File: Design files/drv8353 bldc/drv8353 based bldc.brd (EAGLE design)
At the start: 127 x 127 mm, 117 parts, among them IC1 DRV8353RSRGZT, J3 2X6 FEMALE, J4 B06B-HCMKK

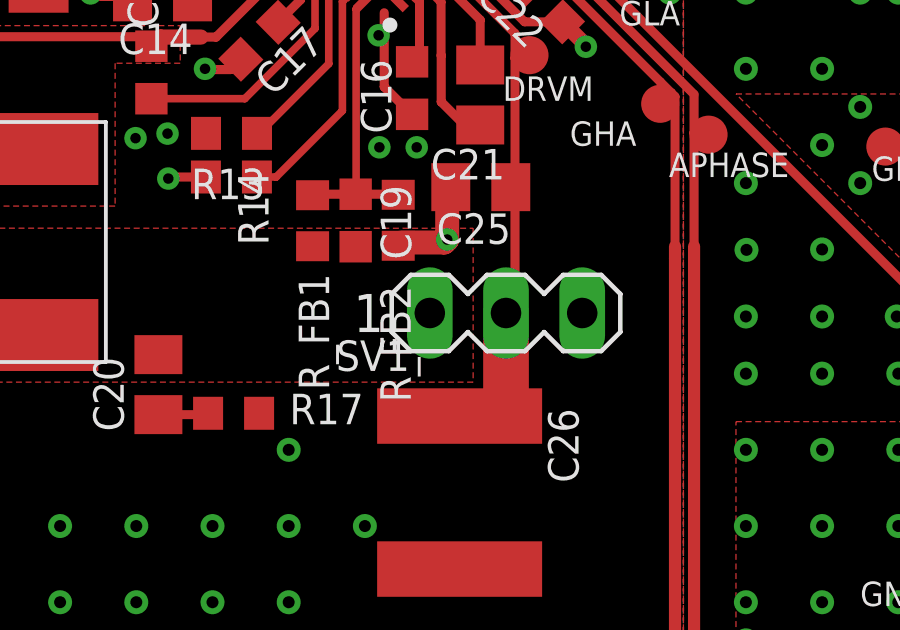
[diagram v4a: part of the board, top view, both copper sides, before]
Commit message: adds 3d  packages for some parts
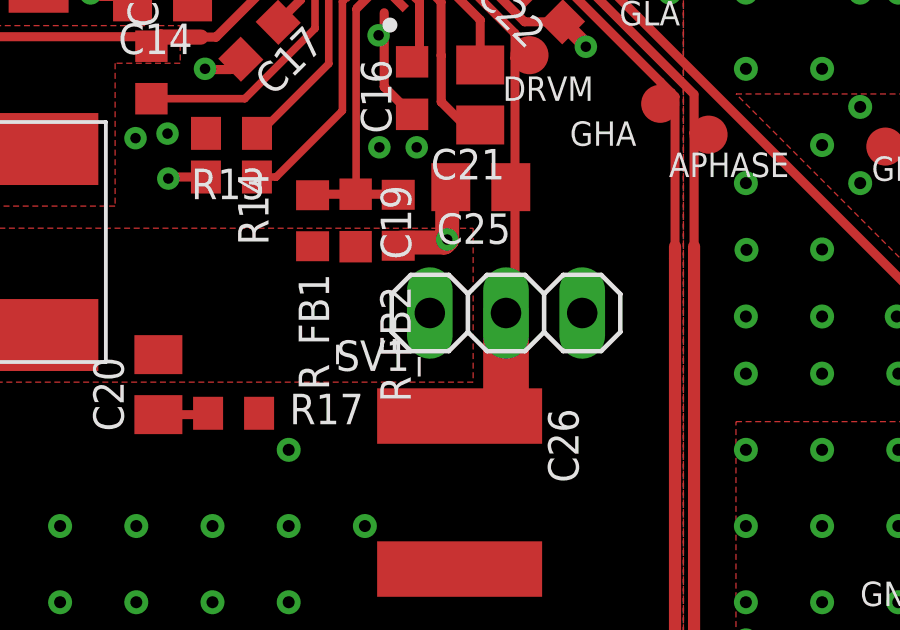
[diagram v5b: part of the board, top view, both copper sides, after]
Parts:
- SV1: device con-lstb:MA03-1 -> pinhead:1X03
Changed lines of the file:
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@@
 <?xml version="1.0" encoding="utf-8"?>
 <!DOCTYPE eagle SYSTEM "eagle.dtd">
-<eagle version="9.5.1">
+<eagle version="9.5.0">
 <drawing>
 <settings>
@@
 </layers>
 <board>
+<fusionsync huburn="a.cGVyc29uYWw6dWUyOTY5NDJi" projecturn="a.cGVyc29uYWw6dWUyOTY5NDJiIzIwMTkxMTI1MjQxNDgzMDA2" f3durn="urn:adsk.wipprod:dm.lineage:7shj7jZ-RWSCfGlzcT_RVg" pcbguid="9bf0e487-037b-48d2-b25e-af9a8d64580e" lastpulledtime="" lastsyncedchangeguid="c1b92a7e-e611-be40-98a8-e297ad73fcdf"/>
 <plain>
 <wire x1="0" y1="0" x2="127" y2="0" width="0" layer="20"/>
@@
 <attribute name="SPICEPREFIX" value="C" x="142.7936" y="162.8696" size="1.778" layer="27" rot="R90" display="off"/>
 </element>
-<element name="C14" library="resistor" library_urn="urn:adsk.eagle:library:348" package="C0805K" package3d_urn="urn:adsk.eagle:package:26201/1" value=".1 uF" x="46.5952" y="77.3122" smashed="yes" rot="R180">
+<element name="C14" library="resistor" library_urn="urn:adsk.eagle:library:348" package="C0805K" package3d_urn="urn:adsk.eagle:package:26201/1" override_package3d_urn="urn:adsk.eagle:package:15402406/2" override_package_urn="urn:adsk.eagle:footprint:25771/1" value=".1 uF" x="46.5952" y="77.3122" smashed="yes" rot="R180">
 <attribute name="NAME" x="47.5952" y="76.4372" size="1.016" layer="25" rot="R180"/>
 </element>
@@
 <attribute name="SPICEPREFIX" value="C" x="170.2138" y="175.658796875" size="1.778" layer="27" rot="R90" display="off"/>
 </element>
-<element name="C22" library="resistor" library_urn="urn:adsk.eagle:library:348" package="C0603K" package3d_urn="urn:adsk.eagle:package:26200/1" value="1 uF" x="59.308421875" y="77.11371875" smashed="yes" rot="R135.1">
+<element name="C22" library="resistor" library_urn="urn:adsk.eagle:library:348" package="C0603K" package3d_urn="urn:adsk.eagle:package:26200/1" override_package3d_urn="urn:adsk.eagle:package:15402361/2" override_package_urn="urn:adsk.eagle:footprint:25770/1" value="1 uF" x="59.308421875" y="77.11371875" smashed="yes" rot="R135.1">
 <attribute name="NAME" x="59.463878125" y="76.268003125" size="1.016" layer="25" rot="R135.1"/>
 </element>
-<element name="C23" library="resistor" library_urn="urn:adsk.eagle:library:348" package="C0603K" package3d_urn="urn:adsk.eagle:package:26200/1" value=".1 uF" x="52.1136" y="89.3542" smashed="yes" rot="R90">
+<element name="C23" library="resistor" library_urn="urn:adsk.eagle:library:348" package="C0603K" package3d_urn="urn:adsk.eagle:package:26200/1" override_package3d_urn="urn:adsk.eagle:package:15402364/2" override_package_urn="urn:adsk.eagle:footprint:25770/1" value=".1 uF" x="52.1136" y="89.3542" smashed="yes" rot="R90">
 <attribute name="NAME" x="53.6734" y="88.0716" size="1.016" layer="25" rot="R90"/>
 </element>
@@
 </element>
 <element name="F1" library="REV BLDC" package="KEYSTONE_MAXI_FUSE_CLIP_3555" value="KEYSTONE_MAXI_FUSE_3555" x="78.3792" y="32.7418" smashed="yes" rot="R180"/>
-<element name="IC1" library="REV BLDC" package="QFN50P700X700X100-49N" value="DRV8353RSRGZT" x="53.8738" y="81.6388" smashed="yes" rot="R135">
+<element name="IC1" library="REV BLDC" package="QFN50P700X700X100-49N" override_package3d_urn="urn:adsk.eagle:package:15402355/2" override_package_urn="urn:adsk.eagle:footprint:15402356/1" value="DRV8353RSRGZT" x="53.8738" y="81.6388" smashed="yes" rot="R135">
 <attribute name="DESCRIPTION" value="100-V Three-Phase Smart Gate Driver With Buck Regulator and Three Current Shunt Amplifiers" x="104.163234375" y="162.461103125" size="1.778" layer="27" rot="R135" display="off"/>
 <attribute name="HEIGHT" value="1mm" x="104.163234375" y="162.461103125" size="1.778" layer="27" rot="R135" display="off"/>
@@
 <attribute name="VALUE" x="10.0144" y="80.9494" size="1.016" layer="27" rot="R270"/>
 </element>
-<element name="SV1" library="con-lstb" library_urn="urn:adsk.eagle:library:162" package="MA03-1" package3d_urn="urn:adsk.eagle:package:8339/1" value="" x="58.0438" y="66.7908" smashed="yes">
-<attribute name="MF" value="" x="132.9738" y="-32.2692" size="1.778" layer="27" display="off"/>
-<attribute name="MPN" value="" x="132.9738" y="-32.2692" size="1.778" layer="27" display="off"/>
+<element name="SV1" library="pinhead" library_urn="urn:adsk.eagle:library:325" package="1X03" package3d_urn="urn:adsk.eagle:package:22458/2" override_package3d_urn="urn:adsk.eagle:package:15402612/2" override_package_urn="urn:adsk.eagle:footprint:8281/1" override_locally_modified="yes" value="" x="58.0438" y="66.7908" smashed="yes">
 <attribute name="NAME" x="52.3796" y="64.8604" size="1.016" layer="25" ratio="10"/>
-<attribute name="OC_FARNELL" value="unknown" x="132.9738" y="-32.2692" size="1.778" layer="27" display="off"/>
-<attribute name="OC_NEWARK" value="unknown" x="132.9738" y="-32.2692" size="1.778" layer="27" display="off"/>
-<attribute name="POPULARITY" value="48" x="132.9738" y="-32.2692" size="1.778" layer="27" display="off"/>
+<attribute name="POPULARITY" value="92" x="132.9738" y="-32.2692" size="1.778" layer="27" display="off"/>
 <attribute name="VALUE" x="54.2338" y="63.8698" size="1.27" layer="27" ratio="10"/>
 </element>
@@
 </note>
 <note version="8.3" severity="warning">
+Since Version 8.3, EAGLE supports Fusion synchronisation.
+This feature will not be available in this version and saving
+the document will break the link to the Fusion PCB feature.
+</note>
+<note version="8.3" severity="warning">
 Since Version 8.3, EAGLE supports URNs for individual library
 assets (packages, symbols, and devices). The URNs of those assets
@@
 will not be understood (or retained) with this version.
 </note>
+<note version="9.4" severity="warning">
+Since Version 9.4, EAGLE supports the overriding of 3D packages
+in schematics and board files. Those overridden 3d packages
+will not be understood (or retained) with this version.
+</note>

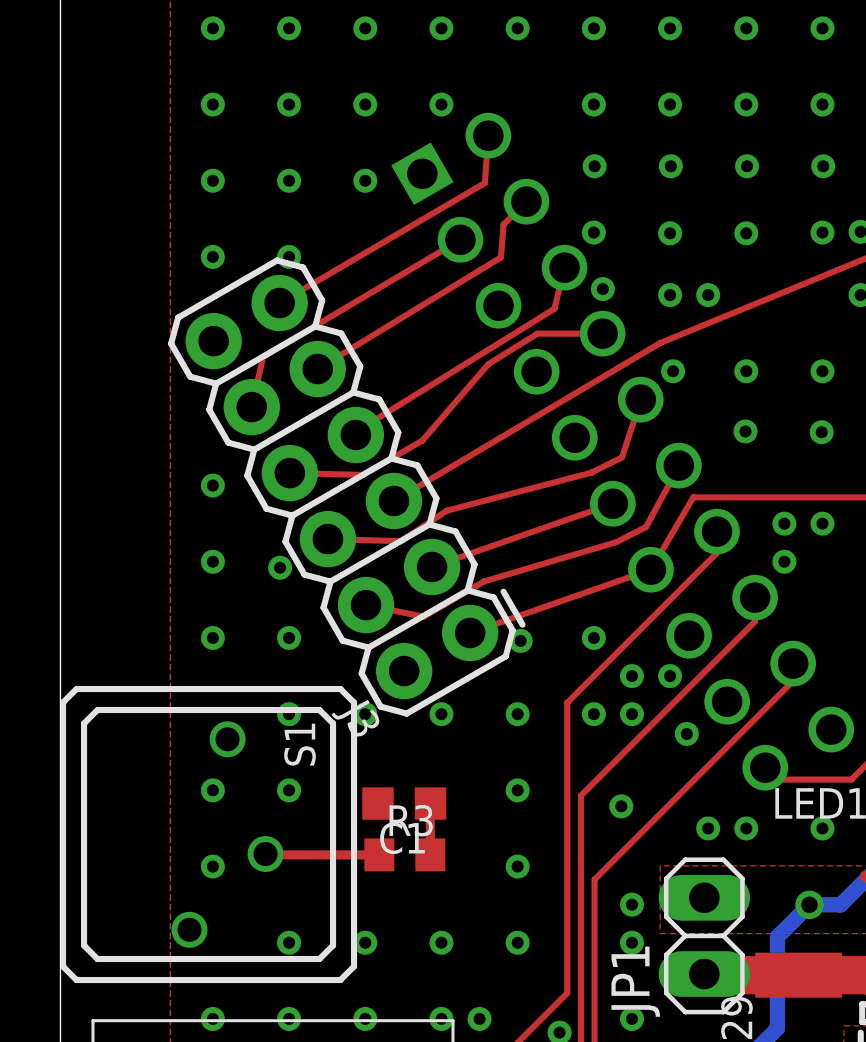
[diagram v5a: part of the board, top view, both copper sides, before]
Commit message: added more 3d packages
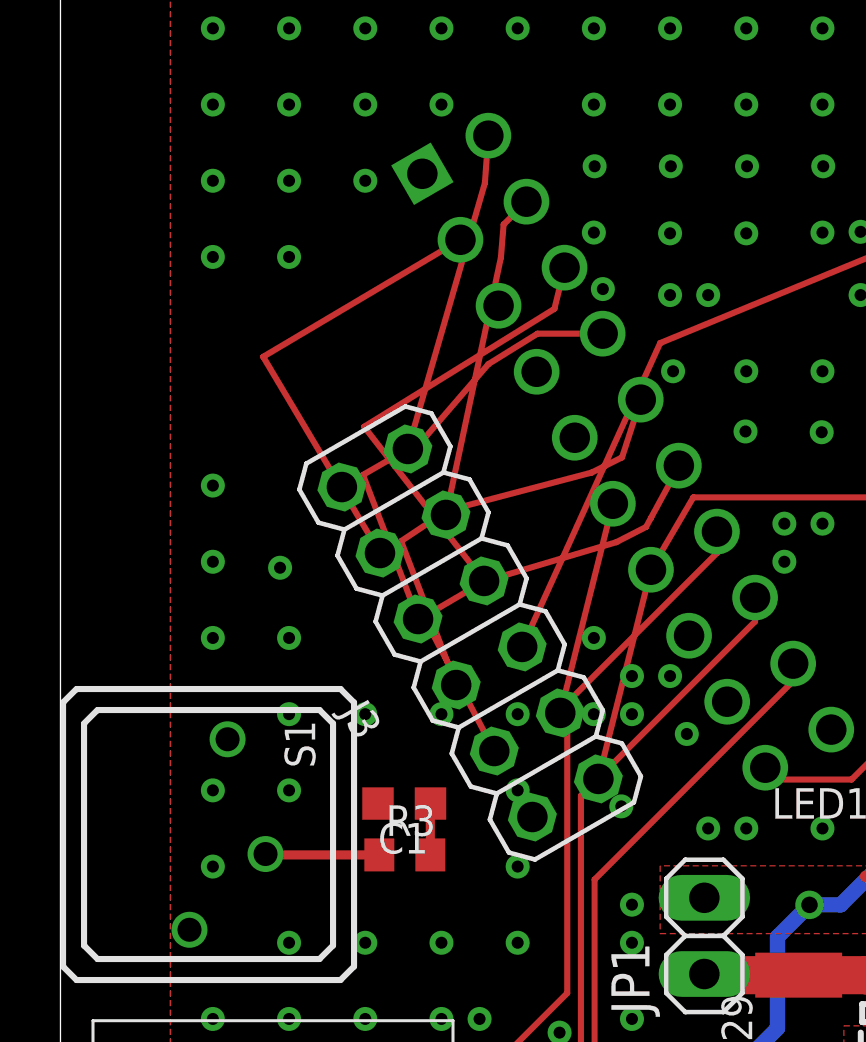
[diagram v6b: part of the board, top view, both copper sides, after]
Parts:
- J3: device SparkFun-Connectors:2X6 -> pinhead:2X06
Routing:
- net INHB: track 47.2 -> 53.3 mm
- net CS: track 53.0 -> 58.9 mm
- net INLC: track 45.5 -> 48.6 mm
- net INLB: track 48.6 -> 51.3 mm
- net INHC: track 47.2 -> 49.9 mm
- net INLA: track 49.6 -> 51.3 mm
- net INHA: track 52.2 -> 53.5 mm
- net SCLK: track 78.3 -> 79.1 mm
- net MOSI: track 41.1 -> 41.9 mm
- net MISO: track 42.9 -> 43.7 mm

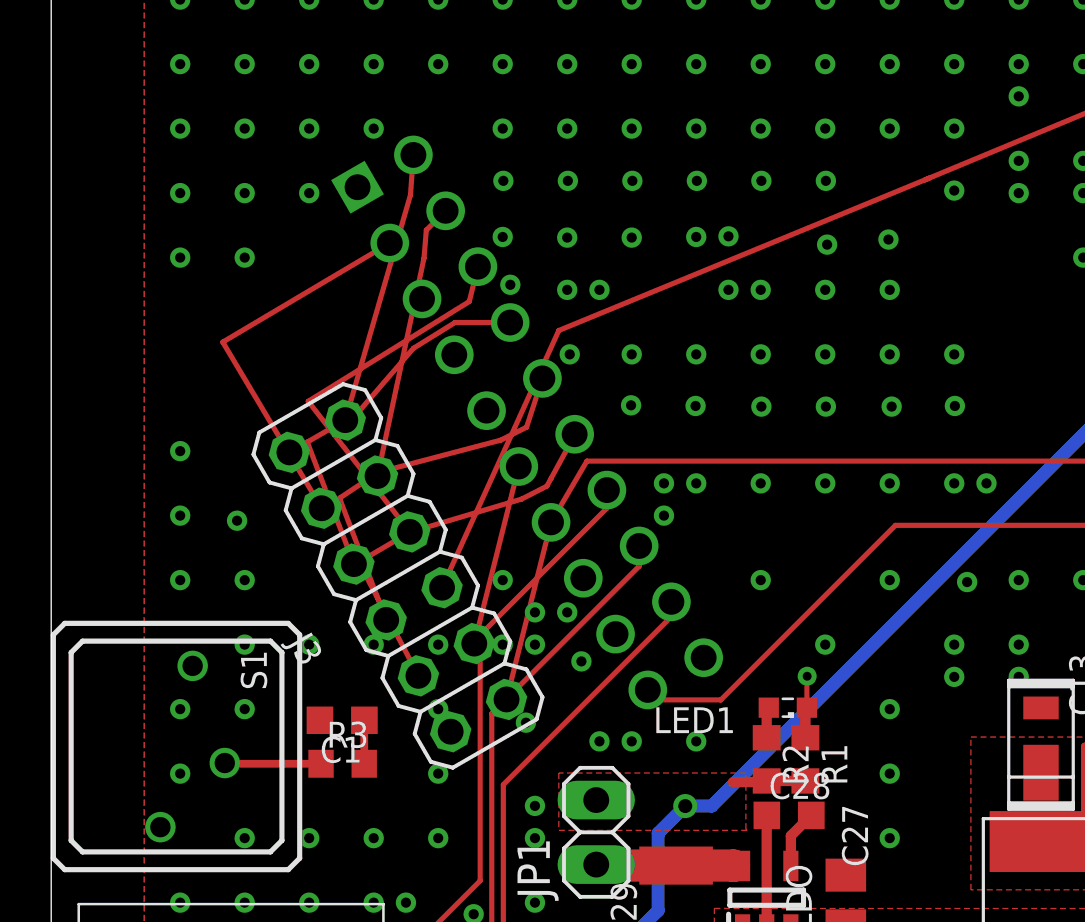
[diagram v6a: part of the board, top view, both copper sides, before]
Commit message: fixed debug header
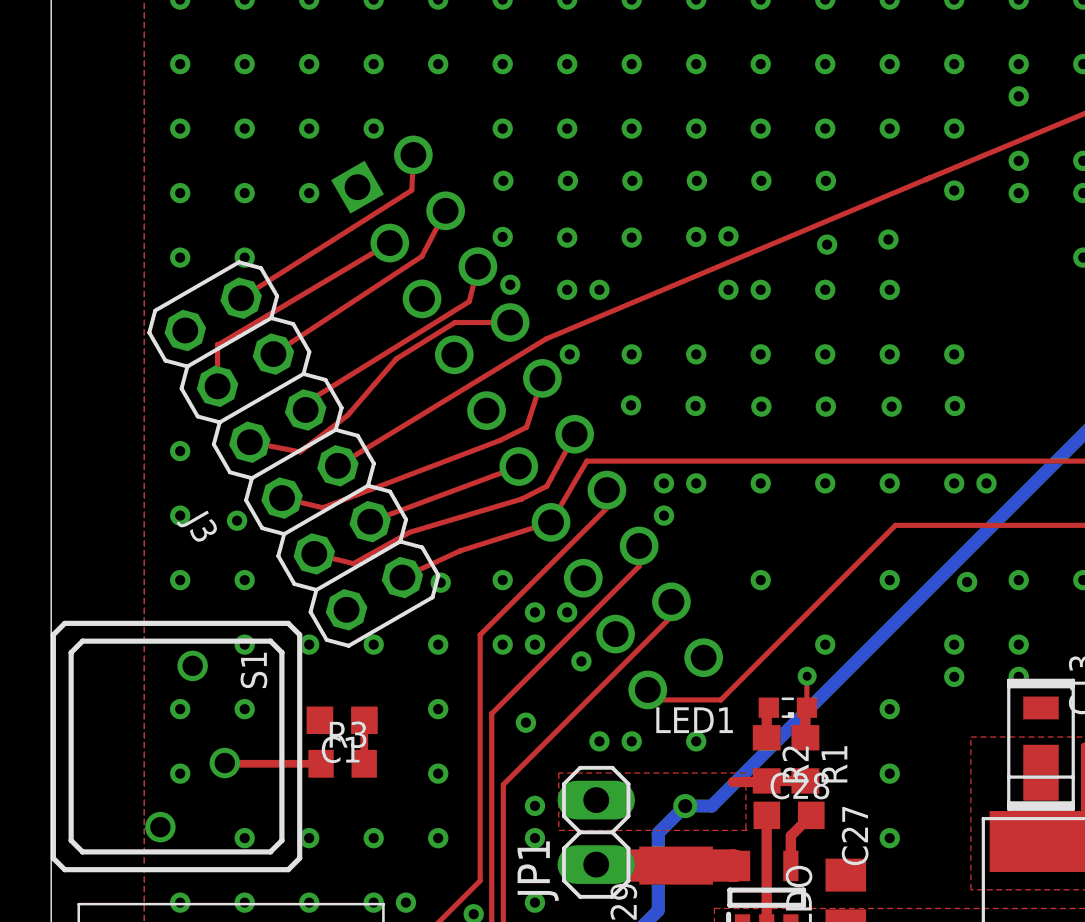
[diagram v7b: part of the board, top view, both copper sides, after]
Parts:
- moved J3 6.31 mm to (9.56, 87.5)
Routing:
- net INHB: track 53.3 -> 47.3 mm
- net CS: track 58.9 -> 53.2 mm
- net INLC: track 48.6 -> 45.3 mm
- net INHC: track 49.9 -> 47.1 mm
- net INLB: track 51.3 -> 48.6 mm
- net INLA: track 51.3 -> 49.3 mm
- net INHA: track 53.5 -> 52.0 mm
- net MOSI: track 41.9 -> 41.0 mm
- net MISO: track 43.7 -> 42.8 mm
- net SCLK: track 79.1 -> 78.2 mm
